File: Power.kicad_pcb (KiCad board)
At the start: 6 copper layers, 53 x 108.8 mm, 289 parts, among them Y1 16M

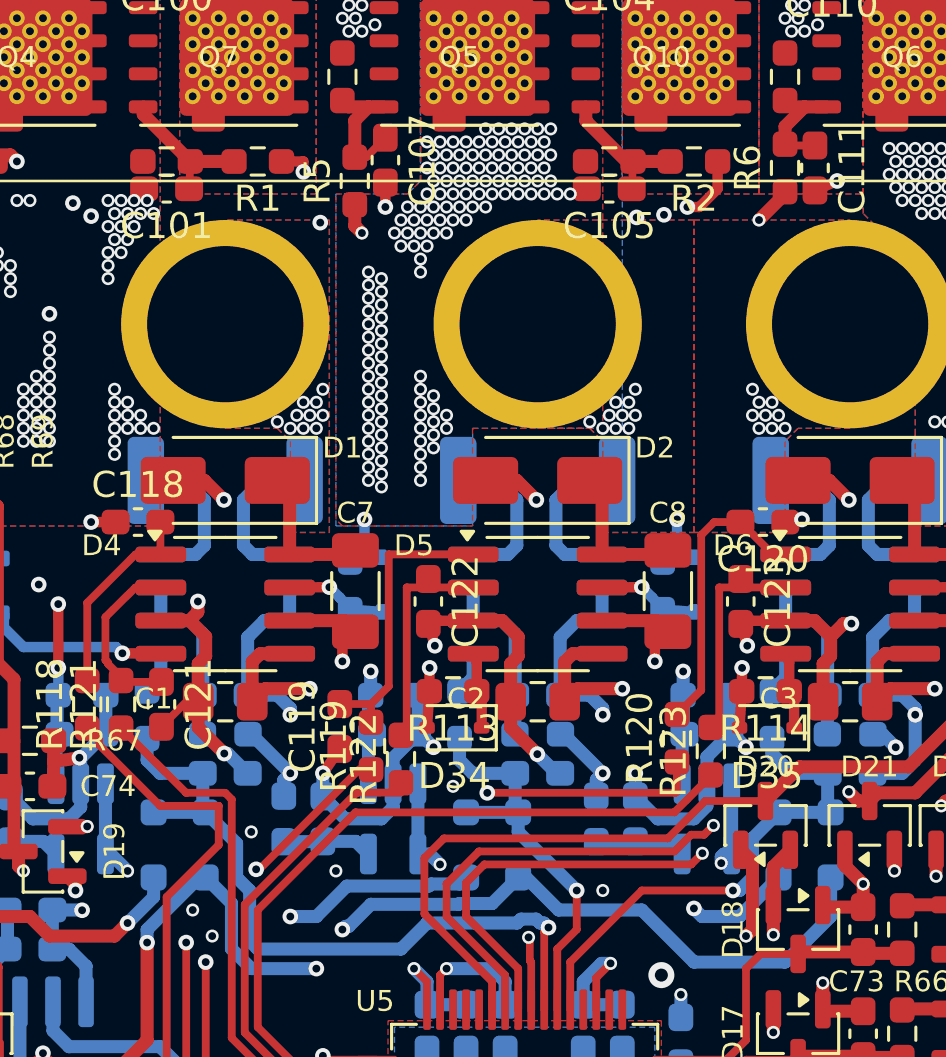
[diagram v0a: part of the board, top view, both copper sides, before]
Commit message: Разводка: изломы 90° срезаны под 45° (29 из 36; 6 внутри пэдов и виа), вход HI D4 переложен прямо
Co-Authored-By: Claude Opus 5.5 <noreply@anthropic.com>
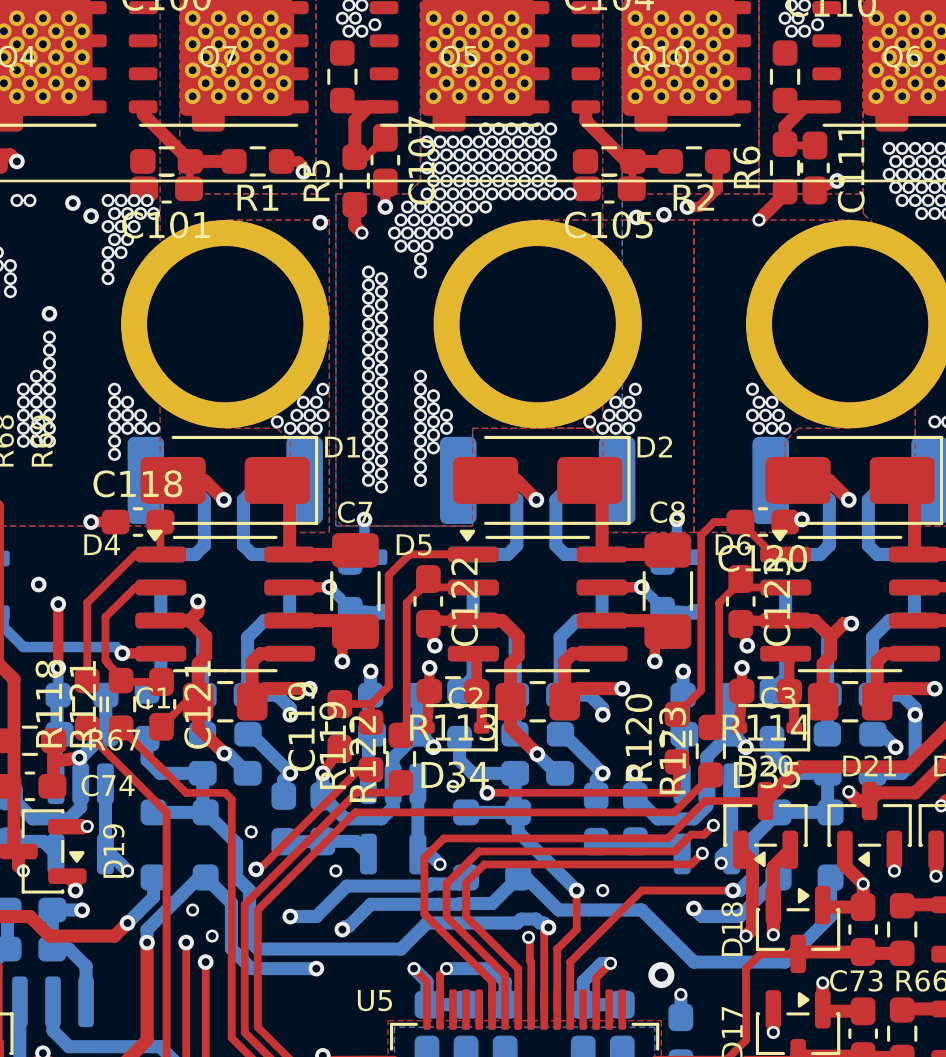
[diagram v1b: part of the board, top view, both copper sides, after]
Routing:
- net +3.3V: track 152.4 -> 148.8 mm
- net /TMR1_CH3: track 27.1 -> 24.2 mm
- net Net-(U1-+): track 39.8 -> 38.7 mm
- net /Driver_2/SW: track 38.0 -> 37.0 mm
- net VDC: track 33.9 -> 32.8 mm
- net /Driver_3/HO: track 34.3 -> 33.7 mm

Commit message: In3 — сплошная земля на всю плату: 152 сегмента (456 мм, 23 цепи) перенесены на In2/In4, DRC 0 ошибок
Co-Authored-By: Claude Opus 5.5 <noreply@anthropic.com>
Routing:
- net /Driver_3/LO: track 32.8 -> 32.6 mm, vias 4 -> 3
